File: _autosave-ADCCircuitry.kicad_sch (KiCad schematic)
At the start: 24 parts, among them J1 Screw_Terminal_01x04, J2 Screw_Terminal_01x04, J3 Screw_Terminal_01x04, J4 Screw_Terminal_01x04, U2 ADS112C04, U3 ADS112C04, U4 ADS112C04, U5 ADS112C04

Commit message: Add valve control
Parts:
- U2, U3, U4, U5: LCSC (none) -> C701615; MPN (none) -> ADS112C04IPWR
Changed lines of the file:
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@@
+			)
+		)
+		(property "MPN" "ADS112C04IPWR"
+			(at 99.06 134.62 0)
+			(effects
+				(font
+					(size 1.27 1.27)
+				)
+				(hide yes)
+			)
+		)
+		(property "LCSC" "C701615"
+			(at 99.06 134.62 0)
+			(effects
+				(font
+					(size 1.27 1.27)
+				)
+				(hide yes)
 			)
 		)
@@
 			)
 		)
+		(property "MPN" "ADS112C04IPWR"
+			(at 99.06 83.82 0)
+			(effects
+				(font
+					(size 1.27 1.27)
+				)
+				(hide yes)
+			)
+		)
+		(property "LCSC" "C701615"
+			(at 99.06 83.82 0)
+			(effects
+				(font
+					(size 1.27 1.27)
+				)
+				(hide yes)
+			)
+		)
 		(pin "2"
 		)
@@
 			)
 		)
+		(property "LCSC" "C701615"
+			(at 220.98 83.82 0)
+			(effects
+				(font
+					(size 1.27 1.27)
+				)
+				(hide yes)
+			)
+		)
+		(property "MPN" "ADS112C04IPWR"
+			(at 220.98 83.82 0)
+			(effects
+				(font
+					(size 1.27 1.27)
+				)
+				(hide yes)
+			)
+		)
 		(pin "2"
 		)
@@
 			(at 220.98 134.62 0)
 			(effects
+				(font
+					(size 1.27 1.27)
+				)
+				(hide yes)
+			)
+		)
+		(property "MPN" "ADS112C04IPWR"
+			(at 220.98 134.62 0)
+			(effects
+				(font
+					(size 1.27 1.27)
+				)
+				(hide yes)
+			)
+		)
+		(property "LCSC" "C701615"
+			(at 220.98 134.62 0)
+			(effects

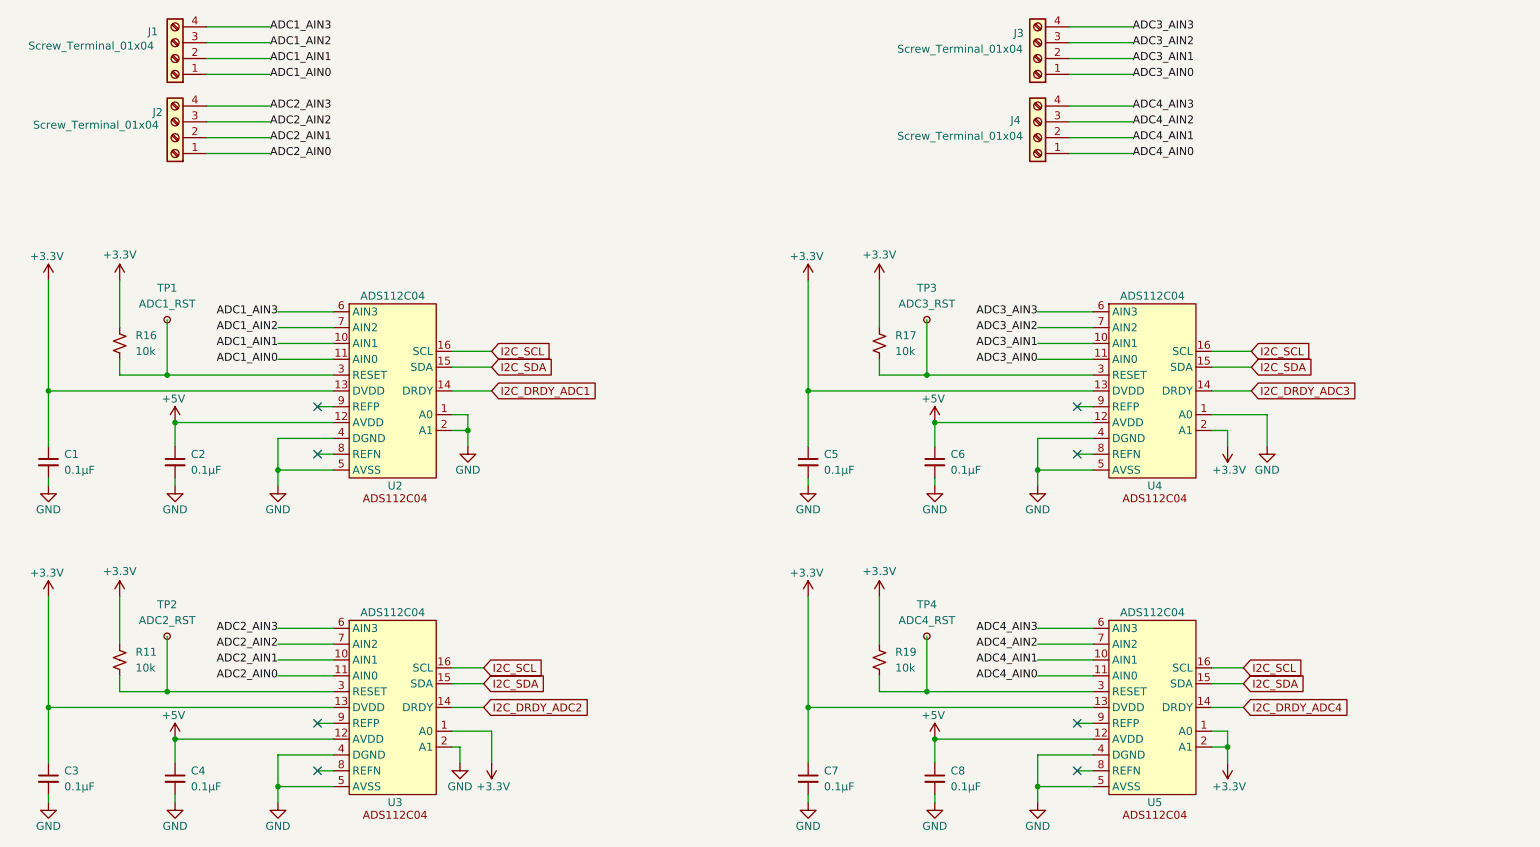
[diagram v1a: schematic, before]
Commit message: Add SAFE +24V
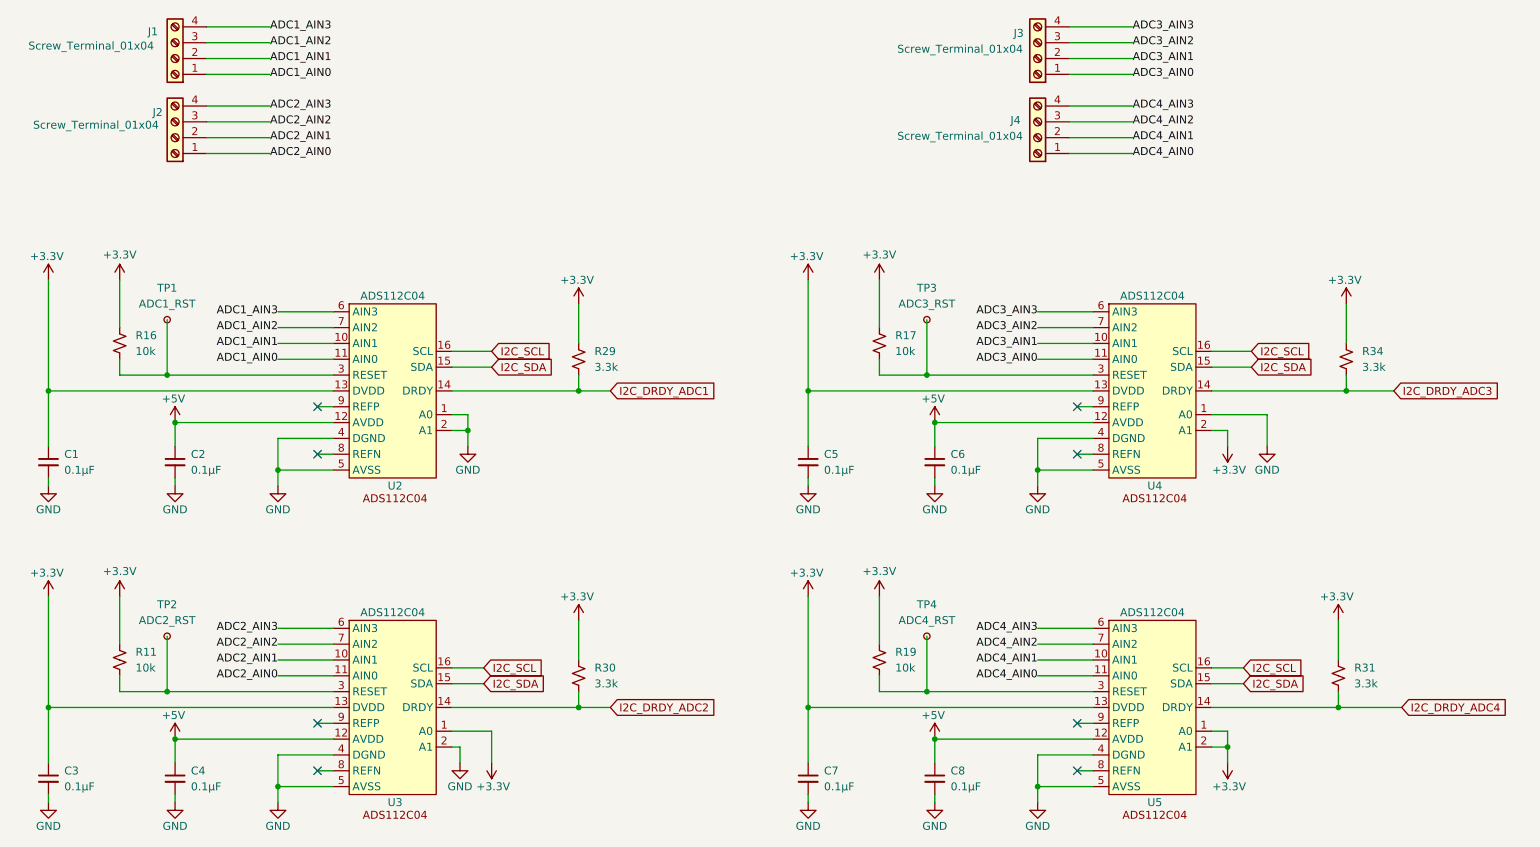
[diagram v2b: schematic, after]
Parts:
- added R29, R30, R31, R34: 3.3k, Resistor_SMD:R_0402_1005Metric, symbol Device:R_Small_US
- J1, J2, J3, J4: Digikey PN (none) -> ED10563-ND
- TP1, TP2, TP3, TP4: footprint (none) -> TestPoint:TestPoint_Pad_D2.0mm
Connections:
- net +3.3V: now also R29.1, R30.1, R31.1, R34.1
- net I2C_DRDY_ADC1: now also R29.2
- net I2C_DRDY_ADC2: now also R30.2
- net I2C_DRDY_ADC3: now also R34.2
- net I2C_DRDY_ADC4: now also R31.2
